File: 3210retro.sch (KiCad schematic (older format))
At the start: 11 parts, among them P101 USB_OTG, P102 BAT, P103 DC, P105 EAR, P106 MIC, P107 HEADPHONE, P108 LSPK, P109 RUMBLE, X101 ANT_GPS, X102 ANT_GSM

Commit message: added Ti WL1807/1837 Module for WLAN and Bluetooth. added Test Points
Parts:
- gave numbers to parts that had none: 1
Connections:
- wire segments 135 -> 134
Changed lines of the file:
@@
 LIBS:micro_sd
 LIBS:h144tc215a
-LIBS:3310retro-cache
+LIBS:WL1807MODGIMOCT
+LIBS:tp
+LIBS:w3006
+LIBS:3210retro-cache
 EELAYER 25 0
 EELAYER END
@@
 encoding utf-8
 Sheet 1 9
-Title "Nokia 3310 Retrofit"
-Date "2016-12-08"
+Title "Nokia 3210 Retrofit"
+Date "2016-12-20"
 Rev "1"
 Comp "www.kurzschluss-blog.de"
@@
 	10100 3400 10300 3400
 $Comp
-L GNDA #PWR103
+L GNDA #PWR104
 U 1 1 58075318
 P 10250 2950
-F 0 "#PWR103" H 10250 2700 50  0001 C CNN
+F 0 "#PWR104" H 10250 2700 50  0001 C CNN
 F 1 "GNDA" H 10250 2800 50  0000 C CNN
 F 2 "" H 10250 2950 50  0000 C CNN
@@
 $EndComp
 Wire Wire Line
-	1350 3200 1350 3450
-Wire Wire Line
-	1350 3450 1350 3500
+	1350 3200 1350 3500
 Wire Wire Line
 	1350 3200 1300 3200
@@
 	10250 4000 10250 3900
 $Comp
-L +3V3 #PWR104
+L +3V3 #PWR105
 U 1 1 5849F049
 P 10250 3900
-F 0 "#PWR104" H 10250 3750 50  0001 C CNN
+F 0 "#PWR105" H 10250 3750 50  0001 C CNN
 F 1 "+3V3" H 10250 4040 50  0000 C CNN
 F 2 "" H 10250 3900 50  0000 C CNN
@@
 $EndComp
 $Comp
-L H144TC215A-V0 X?
+L H144TC215A-V0 X103
 U 1 1 585571AA
 P 1450 5800
-F 0 "X?" H 2050 7600 60  0000 C CNN
+F 0 "X103" H 2050 7600 60  0000 C CNN
 F 1 "H144TC215A-V0" H 1150 7600 60  0000 C CNN
 F 2 "" H 1450 5800 60  0000 C CNN
@@
 	850  7500 850  6000
 $Comp
-L GND #PWR?
+L GND #PWR103
 U 1 1 585679D5
 P 1750 6050
-F 0 "#PWR?" H 1750 5800 50  0001 C CNN
+F 0 "#PWR103" H 1750 5800 50  0001 C CNN
 F 1 "GND" H 1750 5900 50  0000 C CNN
 F 2 "" H 1750 6050 50  0000 C CNN

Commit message: moved to some Bus routing for serveral communication signals on the top sheet. This reduces lines on the top sheet.
Changed 4V boost converter circuit toi use TPS61046 for size reasons
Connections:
- wire segments 134 -> 104
- no-connect marks 0 -> 2
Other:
- moved on the sheet: X103

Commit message: aktuelle Version
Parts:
- P102, P103, P105, P106: footprint (none) -> Pin_Headers:Pin_Header_Straight_2x01
- P107: footprint (none) -> Pin_Headers:Pin_Header_Straight_1x04
- P108: footprint (none) -> Pin_Headers:Pin_Header_Straight_1x02
- P109: footprint buttons:Rumble_Pads -> Pin_Headers:Pin_Header_Straight_1x02
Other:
- note added: "2"
- note added: "3"
- note added: "4"
- note added: "5"
- note added: "50Ohm"
- note added: "6"
- note added: "7"
- note added: "8 / 9"
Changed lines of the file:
@@
 F 0 "P102" H 1100 1450 50  0000 C CNN
 F 1 "BAT" V 1200 1300 50  0000 C CNN
-F 2 "" H 1100 1300 50  0001 C CNN
+F 2 "Pin_Headers:Pin_Header_Straight_2x01" H 1100 1300 50  0001 C CNN
 F 3 "" H 1100 1300 50  0000 C CNN
 	1    1100 1300
@@
 F 0 "P105" H 10500 2000 50  0000 C CNN
 F 1 "EAR" H 10650 1850 60  0000 L CNB
-F 2 "" H 10500 1850 50  0001 C CNN
+F 2 "Pin_Headers:Pin_Header_Straight_2x01" H 10500 1850 50  0001 C CNN
 F 3 "" H 10500 1850 50  0000 C CNN
 	1    10500 1850
@@
 F 0 "P106" H 10500 2400 50  0000 C CNN
 F 1 "MIC" H 10650 2250 60  0000 L CNB
-F 2 "" H 10500 2250 50  0001 C CNN
+F 2 "Pin_Headers:Pin_Header_Straight_2x01" H 10500 2250 50  0001 C CNN
 F 3 "" H 10500 2250 50  0000 C CNN
 	1    10500 2250
@@
 F 0 "P107" H 10500 3000 50  0000 C CNN
 F 1 "HEADPHONE" H 10600 2750 60  0000 L CNB
-F 2 "" H 10500 2750 50  0001 C CNN
+F 2 "Pin_Headers:Pin_Header_Straight_1x04" H 10500 2750 50  0001 C CNN
 F 3 "" H 10500 2750 50  0000 C CNN
 	1    10500 2750
@@
 F 0 "P108" H 10500 3500 50  0000 C CNN
 F 1 "LSPK" H 10650 3350 60  0000 L CNB
-F 2 "" H 10500 3350 50  0001 C CNN
+F 2 "Pin_Headers:Pin_Header_Straight_1x02" H 10500 3350 50  0001 C CNN
 F 3 "" H 10500 3350 50  0000 C CNN
 	1    10500 3350
@@
 	10100 3400 10300 3400
 $Comp
-L GNDA #PWR104
+L GNDA #PWR01
 U 1 1 58075318
 P 10250 2950
-F 0 "#PWR104" H 10250 2700 50  0001 C CNN
+F 0 "#PWR01" H 10250 2700 50  0001 C CNN
 F 1 "GNDA" H 10250 2800 50  0000 C CNN
 F 2 "" H 10250 2950 50  0000 C CNN
@@
 	3350 2100 3650 2100
 $Comp
-L GND #PWR102
+L GND #PWR02
 U 1 1 580A6A61
 P 1650 6050
-F 0 "#PWR102" H 1650 5800 50  0001 C CNN
+F 0 "#PWR02" H 1650 5800 50  0001 C CNN
 F 1 "GND" H 1650 5900 50  0000 C CNN
 F 2 "" H 1650 6050 50  0000 C CNN
@@
 $EndComp
 $Comp
-L GND #PWR101
+L GND #PWR03
 U 1 1 580BB0C9
 P 1350 3500
-F 0 "#PWR101" H 1350 3250 50  0001 C CNN
+F 0 "#PWR03" H 1350 3250 50  0001 C CNN
 F 1 "GND" H 1350 3350 50  0000 C CNN
 F 2 "" H 1350 3500 50  0000 C CNN
@@
 F 0 "P103" H 1100 1850 50  0000 C CNN
 F 1 "DC" V 1200 1700 50  0000 C CNN
-F 2 "" H 1100 1700 50  0001 C CNN
+F 2 "Pin_Headers:Pin_Header_Straight_2x01" H 1100 1700 50  0001 C CNN
 F 3 "" H 1100 1700 50  0000 C CNN
 	1    1100 1700
@@
 F 0 "P109" H 10500 4200 50  0000 C CNN
 F 1 "RUMBLE" H 10650 4050 60  0000 L CNB
-F 2 "buttons:Rumble_Pads" H 10500 4050 50  0001 C CNN
+F 2 "Pin_Headers:Pin_Header_Straight_1x02" H 10500 4050 50  0001 C CNN
 F 3 "" H 10500 4050 50  0000 C CNN
 	1    10500 4050
@@
 	10250 4000 10250 3900
 $Comp
-L +3V3 #PWR105
+L +3V3 #PWR04
 U 1 1 5849F049
 P 10250 3900
-F 0 "#PWR105" H 10250 3750 50  0001 C CNN
+F 0 "#PWR04" H 10250 3750 50  0001 C CNN
 F 1 "+3V3" H 10250 4040 50  0000 C CNN
 F 2 "" H 10250 3900 50  0000 C CNN
@@
 F 0 "X103" H 2250 7600 60  0000 C CNN
 F 1 "H144TC215A-V0" H 1350 7600 60  0000 C CNN
-F 2 "" H 1650 5800 60  0000 C CNN
+F 2 "" H 1650 5800 60  0001 C CNN
 F 3 "" H 1650 5800 60  0000 C CNN
 	1    1650 5800
@@
 	1050 7200 1050 6000
 $Comp
-L GND #PWR103
+L GND #PWR05
 U 1 1 585679D5
 P 1950 6050
-F 0 "#PWR103" H 1950 5800 50  0001 C CNN
+F 0 "#PWR05" H 1950 5800 50  0001 C CNN
 F 1 "GND" H 1950 5900 50  0000 C CNN
 F 2 "" H 1950 6050 50  0000 C CNN
@@
 Wire Wire Line
 	5600 4700 5350 4700
+Text Notes 2600 2100 0    98   ~ 0
+2
+Text Notes 6700 2650 0    98   ~ 0
+5
+Text Notes 6600 5350 0    98   ~ 0
+6
+Text Notes 3700 7550 0    98   ~ 0
+8 / 9
+Text Notes 3200 7250 0    98   ~ 0
+3
+Text Notes 9100 4200 0    98   ~ 0
+4
+Text Notes 6600 7550 0    98   ~ 0
+7
+Wire Notes Line
+	1550 2800 1550 3050
+Wire Notes Line
+	1550 3050 3500 3050
+Wire Notes Line
+	3500 3050 3500 2800
+Wire Notes Line
+	3500 2800 1550 2800
+Text Notes 1600 2900 0    59   ~ 0
+50Ohm
 $EndSCHEMATC

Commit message: display placement
The placement of the display connector is set.
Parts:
- P101: symbol USB_OTG -> USB_OTG-RESCUE-3210retro
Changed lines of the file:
@@
 EESchema Schematic File Version 2
+LIBS:3210retro-rescue
 LIBS:power
 LIBS:device
@@
 $EndComp
 $Comp
-L USB_OTG P101
+L USB_OTG-RESCUE-3210retro P101
 U 1 1 580B8413
 P 1000 3000
@@
 $EndSheet
 $Sheet
-S 5600 3450 1150 1950
+S 5600 4300 1150 1950
 U 580EAE94
 F0 "WiFi/BT Controller" 60
 F1 "WIFI.sch" 60
-F2 "~LINK_UP" O L 5600 4300 60
-F3 "~INT" O L 5600 4400 60
-F4 "~RESET" I L 5600 4500 60
-F5 "GPIO0" I L 5600 4600 60
-F6 "EXT_32K" I L 5600 5100 60
-F7 "BT_EN" I L 5600 5200 60
-F8 "ESP_UART[0..3]" B L 5600 3550 60
-F9 "BT[0..7]" B L 5600 3750 60
-F10 "WLAN_EN" I L 5600 5300 60
-F11 "WL[0..6]" B L 5600 3950 60
-F12 "CH_PD" I L 5600 5000 60
-F13 "GPIO12" B L 5600 4700 60
-F14 "GPIO13" B L 5600 4800 60
+F2 "~LINK_UP" O L 5600 5150 60
+F3 "~INT" O L 5600 5250 60
+F4 "~RESET" I L 5600 5350 60
+F5 "GPIO0" I L 5600 5450 60
+F6 "EXT_32K" I L 5600 5950 60
+F7 "BT_EN" I L 5600 6050 60
+F8 "ESP_UART[0..3]" B L 5600 4400 60
+F9 "BT[0..7]" B L 5600 4600 60
+F10 "WLAN_EN" I L 5600 6150 60
+F11 "WL[0..6]" B L 5600 4800 60
+F12 "CH_PD" I L 5600 5850 60
+F13 "GPIO12" B L 5600 5550 60
+F14 "GPIO13" B L 5600 5650 60
 $EndSheet
 $Comp
@@
 $EndComp
 Wire Wire Line
-	5350 4300 5600 4300
-Wire Wire Line
-	5600 4400 5350 4400
-Wire Wire Line
-	5350 4500 5600 4500
-Wire Wire Line
-	5600 4600 5350 4600
+	5350 5150 5600 5150
+Wire Wire Line
+	5600 5250 5350 5250
+Wire Wire Line
+	5350 5350 5600 5350
+Wire Wire Line
+	5600 5450 5350 5450
 Wire Wire Line
 	10100 4100 10300 4100
@@
 F21 "3V3_PG" I L 3650 2500 60
 F22 "GPS_TX" I R 5350 2700 60
-F23 "~LINK_UP" I R 5350 4300 60
-F24 "~INT" I R 5350 4400 60
-F25 "RESET" O R 5350 4500 60
-F26 "GPIO0" O R 5350 4600 60
+F23 "~LINK_UP" I R 5350 5150 60
+F24 "~INT" I R 5350 5250 60
+F25 "RESET" O R 5350 5350 60
+F26 "GPIO0" O R 5350 5450 60
 F27 "KEY[0..7]" B R 5350 7400 60
 F28 "LED[0..5]" O R 5350 7500 60
-F29 "ESP_UART[0..3]" B R 5350 3550 60
-F30 "BT[0..7]" B R 5350 3750 60
-F31 "WL[0..6]" B R 5350 3950 60
+F29 "ESP_UART[0..3]" B R 5350 4400 60
+F30 "BT[0..7]" B R 5350 4600 60
+F31 "WL[0..6]" B R 5350 4800 60
 F32 "UART[0..3]" B R 5350 2300 60
 F33 "HST_DL[0..1]" B R 5350 2500 60
-F34 "CH_PD" O R 5350 5000 60
-F35 "EXT_32K" O R 5350 5100 60
-F36 "BT_EN" O R 5350 5200 60
-F37 "WLAN_EN" O R 5350 5300 60
-F38 "GPIO12" B R 5350 4700 60
-F39 "GPIO13" B R 5350 4800 60
+F34 "CH_PD" O R 5350 5850 60
+F35 "EXT_32K" O R 5350 5950 60
+F36 "BT_EN" O R 5350 6050 60
+F37 "WLAN_EN" O R 5350 6150 60
+F38 "GPIO12" B R 5350 5550 60
+F39 "GPIO13" B R 5350 5650 60
 $EndSheet
 Wire Wire Line
@@
 	5350 7400 5600 7400
 Wire Bus Line
-	5350 3550 5600 3550
+	5350 4400 5600 4400
 Wire Bus Line
 	6650 1850 5900 1850
@@
 NoConn ~ 1750 6000
 Wire Bus Line
-	5600 3950 5350 3950
-Wire Bus Line
-	5350 3750 5600 3750
-Wire Wire Line
-	5350 5000 5600 5000
-Wire Wire Line
-	5600 5100 5350 5100
-Wire Wire Line
-	5350 5200 5600 5200
-Wire Wire Line
-	5600 5300 5350 5300
-Wire Wire Line
-	5350 4800 5600 4800
-Wire Wire Line
-	5600 4700 5350 4700
+	5600 4800 5350 4800
+Wire Bus Line
+	5350 4600 5600 4600
+Wire Wire Line
+	5350 5850 5600 5850
+Wire Wire Line
+	5600 5950 5350 5950
+Wire Wire Line
+	5350 6050 5600 6050
+Wire Wire Line
+	5600 6150 5350 6150
+Wire Wire Line
+	5350 5650 5600 5650
+Wire Wire Line
+	5600 5550 5350 5550
 Text Notes 2600 2100 0    98   ~ 0
 2
 Text Notes 6700 2650 0    98   ~ 0
 5
-Text Notes 6600 5350 0    98   ~ 0
+Text Notes 6600 6200 0    98   ~ 0
 6
 Text Notes 3700 7550 0    98   ~ 0

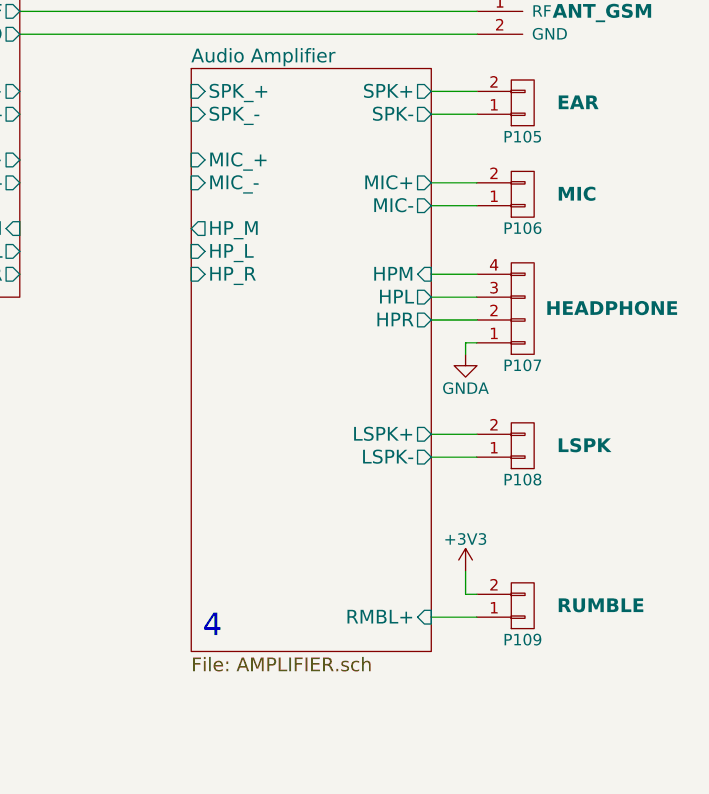
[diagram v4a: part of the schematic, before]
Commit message: added some audio circuitry
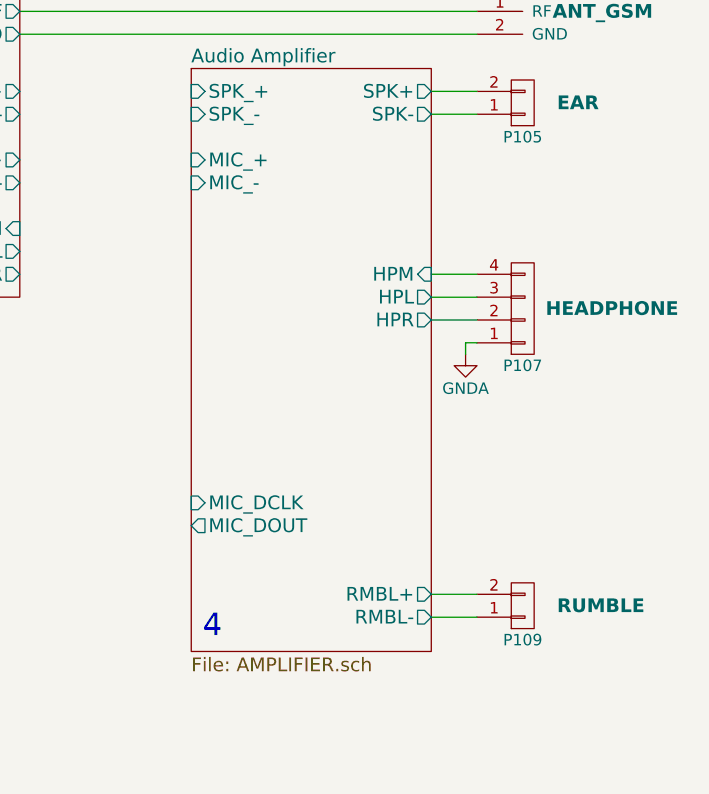
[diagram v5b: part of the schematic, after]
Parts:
- removed P106: MIC, Pin_Headers:Pin_Header_Straight_2x01, symbol CONN_01X02
- removed P108: LSPK, Pin_Headers:Pin_Header_Straight_1x02, symbol CONN_01X02
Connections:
- net +3V3 is gone; now on net Audio Amplifier/RMBL+: P109.2 (P2)
- net Audio Amplifier/RMBL+: no longer P109.1 (P1)
- new net Audio Amplifier/RMBL-: P109.1 (P1)
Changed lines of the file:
@@
 LIBS:w3006
 LIBS:tps61046
+LIBS:mp34dt01tr
+LIBS:drv8601
+LIBS:lm4930
+LIBS:ts5a22366
 LIBS:3210retro-cache
 EELAYER 25 0
@@
 F4 "MIC_+" I L 9050 2100 60
 F5 "MIC_-" I L 9050 2200 60
-F6 "HP_M" O L 9050 2400 60
-F7 "HP_L" I L 9050 2500 60
-F8 "HP_R" I L 9050 2600 60
 F9 "SPK+" O R 10100 1800 60
 F10 "SPK-" O R 10100 1900 60
-F11 "MIC+" O R 10100 2200 60
-F12 "MIC-" O R 10100 2300 60
 F13 "HPM" I R 10100 2600 60
 F14 "HPL" O R 10100 2700 60
 F15 "HPR" O R 10100 2800 60
-F16 "LSPK+" O R 10100 3300 60
-F17 "LSPK-" O R 10100 3400 60
-F18 "RMBL+" I R 10100 4100 60
+F18 "RMBL+" O R 10100 4000 60
+F19 "MIC_DCLK" I L 9050 3600 60
+F20 "MIC_DOUT" O L 9050 3700 60
+F21 "RMBL-" O R 10100 4100 60
 $EndSheet
 $Comp
@@
 $EndComp
 $Comp
-L CONN_01X02 P106
-U 1 1 58071B80
-P 10500 2250
-F 0 "P106" H 10500 2400 50  0000 C CNN
-F 1 "MIC" H 10650 2250 60  0000 L CNB
-F 2 "Pin_Headers:Pin_Header_Straight_2x01" H 10500 2250 50  0001 C CNN
-F 3 "" H 10500 2250 50  0000 C CNN
-	1    10500 2250
-	1    0    0    1
-$EndComp
-$Comp
 L CONN_01X04 P107
 U 1 1 5807200E
@@
 	1    0    0    1
 $EndComp
-$Comp
-L CONN_01X02 P108
-U 1 1 580722B0
-P 10500 3350
-F 0 "P108" H 10500 3500 50  0000 C CNN
-F 1 "LSPK" H 10650 3350 60  0000 L CNB
-F 2 "Pin_Headers:Pin_Header_Straight_1x02" H 10500 3350 50  0001 C CNN
-F 3 "" H 10500 3350 50  0000 C CNN
-	1    10500 3350
-	1    0    0    1
-$EndComp
 Wire Wire Line
 	10100 1800 10300 1800
@@
 	10100 1900 10300 1900
 Wire Wire Line
-	10300 2200 10100 2200
-Wire Wire Line
-	10100 2300 10300 2300
-Wire Wire Line
 	10300 2600 10100 2600
 Wire Wire Line
@@
 Wire Wire Line
 	10300 2800 10100 2800
-Wire Wire Line
-	10100 3300 10300 3300
-Wire Wire Line
-	10100 3400 10300 3400
 $Comp
 L GNDA #PWR01
@@
 	10100 4100 10300 4100
 Wire Wire Line
-	10300 4000 10250 4000
-Wire Wire Line
-	10250 4000 10250 3900
-$Comp
-L +3V3 #PWR04
-U 1 1 5849F049
-P 10250 3900
-F 0 "#PWR04" H 10250 3750 50  0001 C CNN
-F 1 "+3V3" H 10250 4040 50  0000 C CNN
-F 2 "" H 10250 3900 50  0000 C CNN
-F 3 "" H 10250 3900 50  0000 C CNN
-	1    10250 3900
-	1    0    0    -1
-$EndComp
+	10100 4000 10300 4000
 $Comp
 L H144TC215A-V0 X103

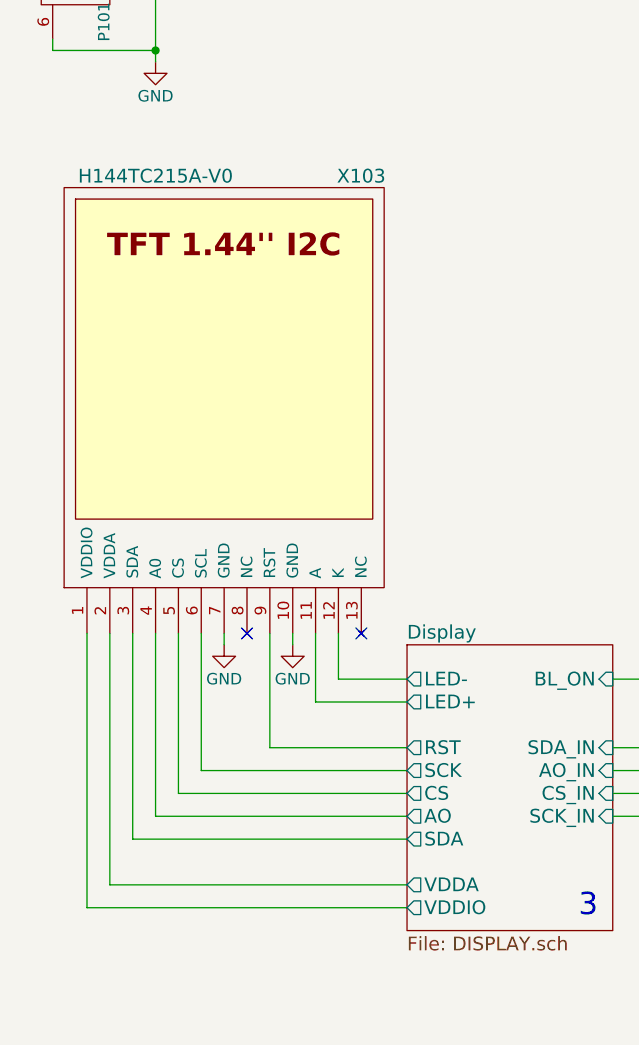
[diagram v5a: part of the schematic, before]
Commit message: Prepare Display change
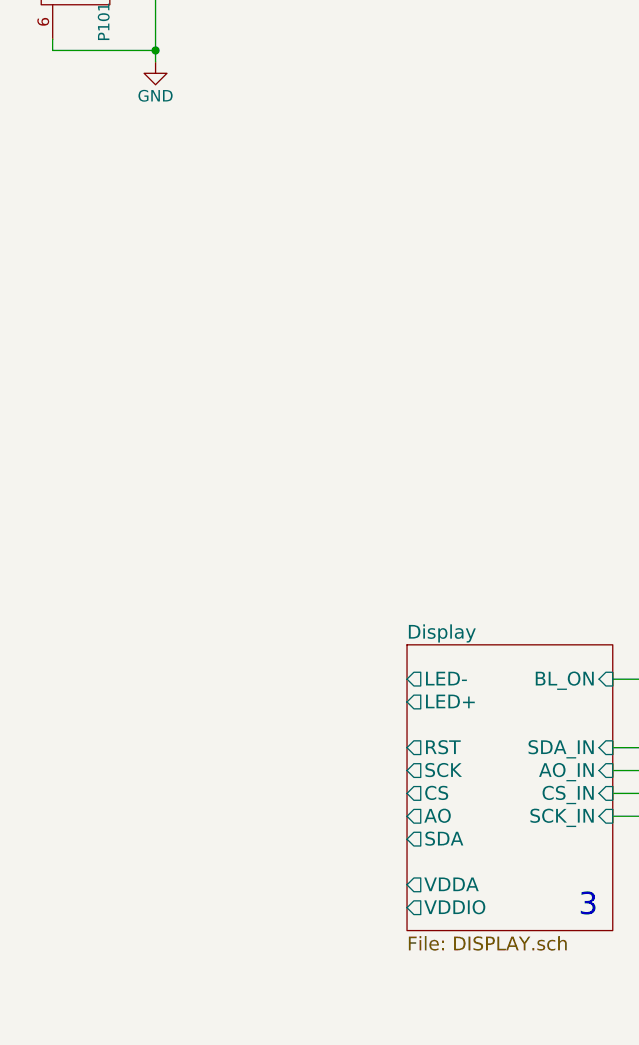
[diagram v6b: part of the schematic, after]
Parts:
- removed X103: H144TC215A-V0, symbol H144TC215A-V0
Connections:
- no-connect marks 2 -> 0
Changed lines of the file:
@@
 F4 "MIC_+" I L 9050 2100 60
 F5 "MIC_-" I L 9050 2200 60
-F9 "SPK+" O R 10100 1800 60
-F10 "SPK-" O R 10100 1900 60
-F13 "HPM" I R 10100 2600 60
-F14 "HPL" O R 10100 2700 60
-F15 "HPR" O R 10100 2800 60
-F18 "RMBL+" O R 10100 4000 60
-F19 "MIC_DCLK" I L 9050 3600 60
-F20 "MIC_DOUT" O L 9050 3700 60
-F21 "RMBL-" O R 10100 4100 60
+F6 "SPK+" O R 10100 1800 60
+F7 "SPK-" O R 10100 1900 60
+F8 "HPM" I R 10100 2600 60
+F9 "HPL" O R 10100 2700 60
+F10 "HPR" O R 10100 2800 60
+F11 "RMBL+" O R 10100 4000 60
+F12 "MIC_DCLK" I L 9050 3600 60
+F13 "MIC_DOUT" O L 9050 3700 60
+F14 "RMBL-" O R 10100 4100 60
 $EndSheet
 $Comp
@@
 Wire Wire Line
 	3350 2100 3650 2100
-$Comp
-L GND #PWR02
-U 1 1 580A6A61
-P 1650 6050
-F 0 "#PWR02" H 1650 5800 50  0001 C CNN
-F 1 "GND" H 1650 5900 50  0000 C CNN
-F 2 "" H 1650 6050 50  0000 C CNN
-F 3 "" H 1650 6050 50  0000 C CNN
-	1    1650 6050
-	1    0    0    -1
-$EndComp
 $Comp
 L USB_OTG-RESCUE-3210retro P101
@@
 Wire Wire Line
 	10100 4000 10300 4000
-$Comp
-L H144TC215A-V0 X103
-U 1 1 585571AA
-P 1650 5800
-F 0 "X103" H 2250 7600 60  0000 C CNN
-F 1 "H144TC215A-V0" H 1350 7600 60  0000 C CNN
-F 2 "" H 1650 5800 60  0001 C CNN
-F 3 "" H 1650 5800 60  0000 C CNN
-	1    1650 5800
-	1    0    0    -1
-$EndComp
-Wire Wire Line
-	2450 6200 2150 6200
-Wire Wire Line
-	2150 6200 2150 6000
-Wire Wire Line
-	2050 6000 2050 6300
-Wire Wire Line
-	2050 6300 2450 6300
-Wire Wire Line
-	2450 6500 1850 6500
-Wire Wire Line
-	1850 6500 1850 6000
-Wire Wire Line
-	1550 6000 1550 6600
-Wire Wire Line
-	1550 6600 2450 6600
-Wire Wire Line
-	2450 6700 1450 6700
-Wire Wire Line
-	1450 6700 1450 6000
-Wire Wire Line
-	1350 6000 1350 6800
-Wire Wire Line
-	1350 6800 2450 6800
-Wire Wire Line
-	2450 6900 1250 6900
-Wire Wire Line
-	1250 6900 1250 6000
-Wire Wire Line
-	1150 6000 1150 7100
-Wire Wire Line
-	1150 7100 2450 7100
-Wire Wire Line
-	2450 7200 1050 7200
-Wire Wire Line
-	1050 7200 1050 6000
-$Comp
-L GND #PWR05
-U 1 1 585679D5
-P 1950 6050
-F 0 "#PWR05" H 1950 5800 50  0001 C CNN
-F 1 "GND" H 1950 5900 50  0000 C CNN
-F 2 "" H 1950 6050 50  0000 C CNN
-F 3 "" H 1950 6050 50  0000 C CNN
-	1    1950 6050
-	1    0    0    -1
-$EndComp
-Wire Wire Line
-	1950 6050 1950 6000
-Wire Wire Line
-	1650 6050 1650 6000
 Wire Wire Line
 	3650 6500 3350 6500
@@
 Wire Bus Line
 	6100 2500 5350 2500
-NoConn ~ 2250 6000
-NoConn ~ 1750 6000
 Wire Bus Line
 	5600 4800 5350 4800
